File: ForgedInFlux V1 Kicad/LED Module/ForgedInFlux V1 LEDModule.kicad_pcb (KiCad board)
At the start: 2 copper layers, 42 x 82 mm, 31 parts

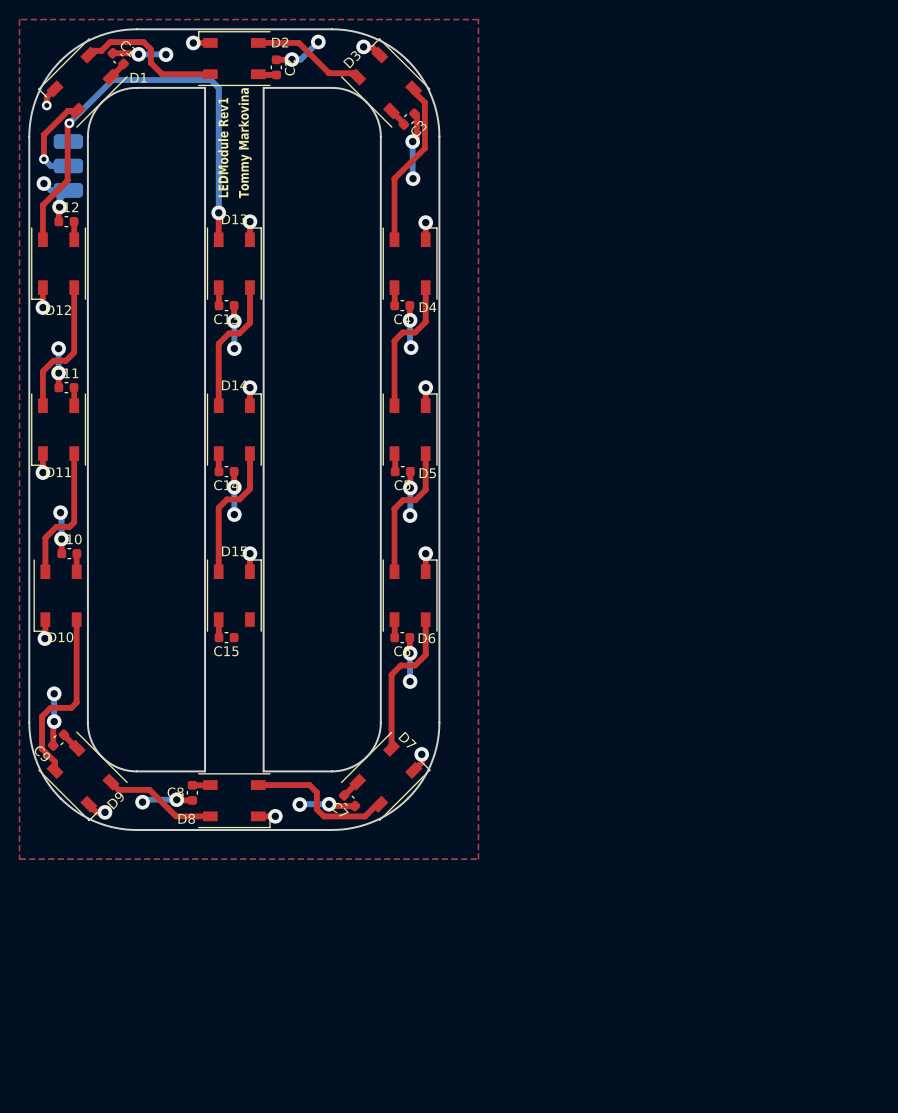
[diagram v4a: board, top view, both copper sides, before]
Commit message: Redesigned PCB
- Components changed for hand solderable parts
- Resistor in future will need to be exchanged for one that can handle more wattage.
- In future more clearance will be needed for top right LED.
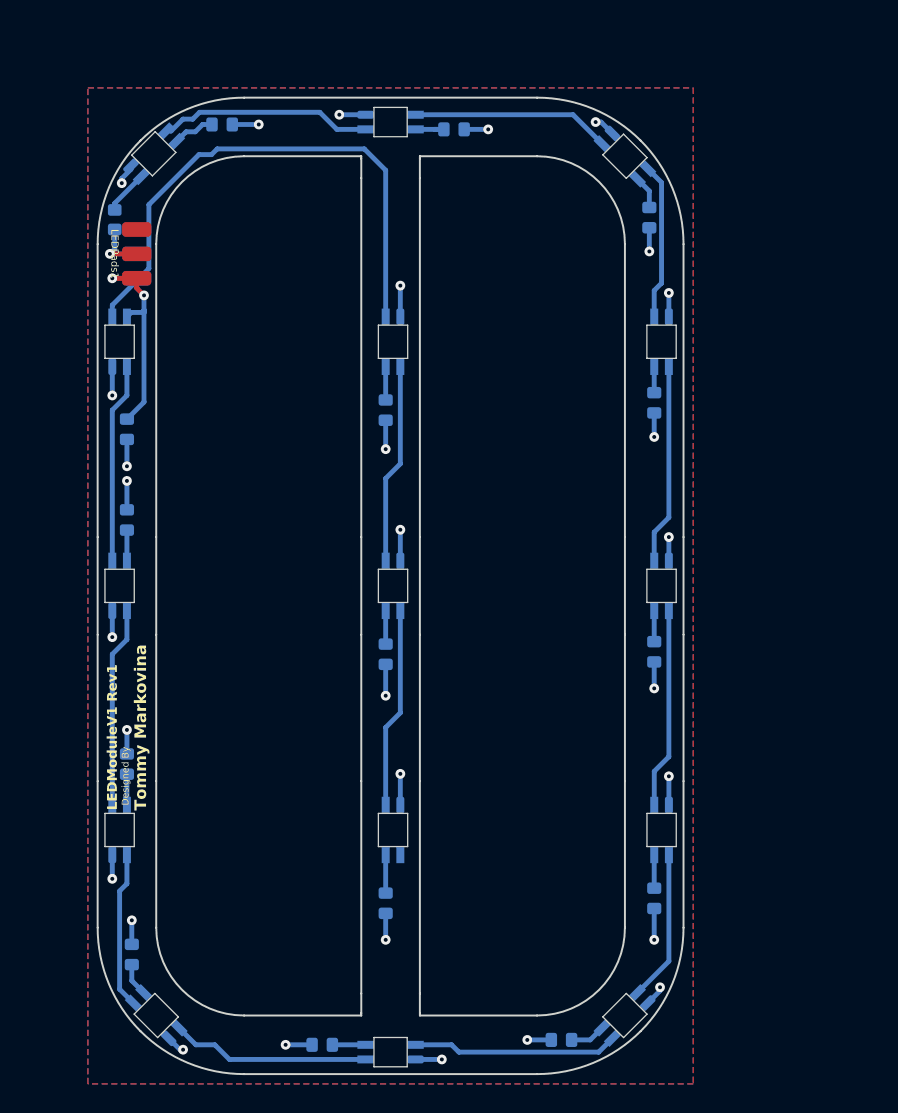
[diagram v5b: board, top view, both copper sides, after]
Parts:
- removed D1, D10, D11, D12, D13, D14, D15, D2, D3, D4, D5, D6, D7, D8, D9: SK6812, LED_SMD:LED_SK6812_PLCC4_5.0x5.0mm_P3.2mm
- added LED1: SK6812MINI-E, LEDModuleLibrary:SK6812-MINI-E, B.Cu at (25.8, 25.8)
- added LED10: SK6812MINI-E, LEDModuleLibrary:SK6812-MINI-E, B.Cu at (22.2, 95.0)
- added LED11: SK6812MINI-E, LEDModuleLibrary:SK6812-MINI-E, B.Cu at (22.2, 70.0)
- added LED12: SK6812MINI-E, LEDModuleLibrary:SK6812-MINI-E, B.Cu at (22.2, 45.0)
- added LED13: SK6812MINI-E, LEDModuleLibrary:SK6812-MINI-E, B.Cu at (50.2, 45.0)
- added LED14: SK6812MINI-E, LEDModuleLibrary:SK6812-MINI-E, B.Cu at (50.2, 70.0)
- added LED15: SK6812MINI-E, LEDModuleLibrary:SK6812-MINI-E, B.Cu at (50.2, 95.0)
- added LED2: SK6812MINI-E, LEDModuleLibrary:SK6812-MINI-E, B.Cu at (50.0, 22.5)
- added LED3: SK6812MINI-E, LEDModuleLibrary:SK6812-MINI-E, B.Cu at (74.0, 26.0)
- added LED4: SK6812MINI-E, LEDModuleLibrary:SK6812-MINI-E, B.Cu at (77.8, 45.0)
- added LED5: SK6812MINI-E, LEDModuleLibrary:SK6812-MINI-E, B.Cu at (77.8, 70.0)
- added LED6: SK6812MINI-E, LEDModuleLibrary:SK6812-MINI-E, B.Cu at (77.8, 95.0)
- added LED7: SK6812MINI-E, LEDModuleLibrary:SK6812-MINI-E, B.Cu at (74.0, 114.0)
- added LED8: SK6812MINI-E, LEDModuleLibrary:SK6812-MINI-E, B.Cu at (50.0, 117.8)
- added LED9: SK6812MINI-E, LEDModuleLibrary:SK6812-MINI-E, B.Cu at (26.0, 114.0)
- added R1: 220R, Resistor_SMD:R_0805_2012Metric_Pad1.20x1.40mm_HandSolder, B.Cu at (21.8, 32.5)
- C1, C10, C11, C12, C13, C14, C15, C2, C3, C4, C5, C6, C7, C8, C9: footprint Capacitor_SMD:C_0603_1608Metric -> Capacitor_SMD:C_0805_2012Metric_Pad1.18x1.45mm_HandSolder; moved to B.Cu
- LEDPads1: moved to F.Cu
- moved C6 37.1 mm to (77.0, 102.0), turned to -90 degrees
- moved C7 32.7 mm to (67.5, 116.5), turned to 180 degrees
- moved C15 31.7 mm to (49.5, 102.5), turned to -90 degrees
- moved C5 31.7 mm to (77.0, 76.8), turned to -90 degrees
- moved C8 29.0 mm to (43.0, 117.0), turned to 180 degrees
- moved C4 27.7 mm to (77.0, 51.2), turned to -90 degrees
- moved C3 26.6 mm to (76.5, 32.3), turned to -90 degrees
- moved C14 24.8 mm to (49.5, 77.0), turned to -90 degrees
- moved C9 23.2 mm to (23.5, 107.8), turned to 90 degrees
- moved C10 22.3 mm to (23.0, 88.2), turned to 90 degrees
- moved C12 22.1 mm to (23.0, 54.0), turned to -90 degrees
- moved C13 19.5 mm to (49.5, 52.0), turned to -90 degrees
- moved C2 19.3 mm to (56.5, 23.2), turned to 0 degrees
- moved C11 14.9 mm to (23.0, 63.2), turned to 90 degrees
- moved C1 12.6 mm to (32.8, 22.8), turned to 0 degrees
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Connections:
- C1 pad 2: Net-(D1-VDD) -> GND
- C10 pad 2: Net-(D10-VDD) -> GND
- C11 pad 2: Net-(D11-VDD) -> GND
- C12 pad 2: Net-(D12-VDD) -> GND
- C13 pad 2: Net-(D13-VDD) -> GND
- C14 pad 2: Net-(D14-VDD) -> GND
- C15 pad 2: Net-(D15-VDD) -> GND
- C2 pad 2: Net-(D2-VDD) -> GND
- C3 pad 2: Net-(D3-VDD) -> GND
- C4 pad 2: Net-(D4-VDD) -> GND
- C5 pad 2: Net-(D5-VDD) -> GND
- C6 pad 2: Net-(D6-VDD) -> GND
- C7 pad 2: Net-(D7-VDD) -> GND
- C8 pad 2: Net-(D8-VDD) -> GND
- C9 pad 2: Net-(D9-VDD) -> GND
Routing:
- net Net-(LED12-DOUT): track 0.00 -> 55.6 mm
- net GND: track 28.5 -> 80.1 mm, vias 15 -> 30
- net Net-(D12-DOUT): track 46.1 -> 0.00 mm, vias 2 -> 0
- net Net-(LED1-DOUT): track 0.00 -> 21.9 mm
- net Net-(LED7-DOUT): track 0.00 -> 21.1 mm
- net Net-(LED13-DOUT): track 0.00 -> 20.5 mm
- net Net-(LED4-DOUT): track 0.00 -> 20.5 mm
- net Net-(LED14-DOUT): track 0.00 -> 20.5 mm
- net Net-(LED11-DOUT): track 0.00 -> 20.5 mm
- net Net-(LED10-DOUT): track 0.00 -> 20.5 mm
- net Net-(LED5-DOUT): track 0.00 -> 20.5 mm
- net Net-(LED8-DOUT): track 0.00 -> 20.5 mm
- net Net-(LED2-DOUT): track 0.00 -> 20.3 mm
- net Net-(D10-DIN): track 18.7 -> 0.00 mm
- net Net-(D3-DOUT): track 17.2 -> 0.00 mm
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- added copper zone on B.Cu, net +5V
- added copper zone on F.Cu, net GND
- removed copper zone on F.Cu, net +5V
- removed copper zone on B.Cu, net GND
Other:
- board size 42 x 82 mm -> 60 x 100 mm
- board text added: "Designed By"
- board text added: "LEDModuleV1 Rev1"
- board text removed: "LEDModule Rev1"

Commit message: Updated design
- Full 1w SMD Resistor
- Satsified tolerances on LEDS and board edgecuts.
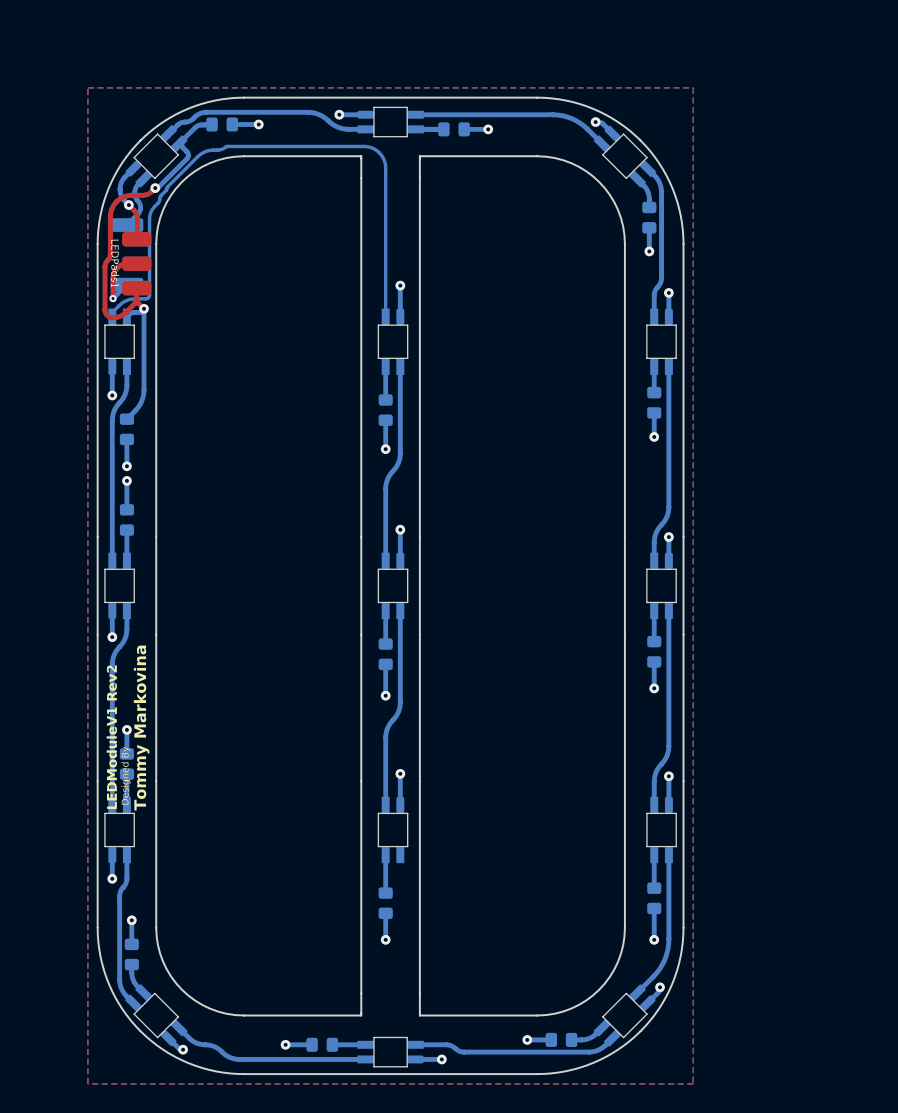
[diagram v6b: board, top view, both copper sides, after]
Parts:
- R1: footprint Resistor_SMD:R_0805_2012Metric_Pad1.20x1.40mm_HandSolder -> Resistor_SMD:R_2512_6332Metric_Pad1.40x3.35mm_HandSolder
- moved R1 3.81 mm to (23.0, 36.1)
- moved LEDPads1 1.00 mm to (24.0, 39.5)
- moved LED1 0.35 mm to (26.0, 26.0)
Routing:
- net +5V: track 67.7 -> 91.7 mm
- net GND: track 80.1 -> 86.2 mm
- net LEDData: track 5.46 -> 7.36 mm
- net Net-(LED1-DIN): track 4.20 -> 5.73 mm
- net Net-(LED12-DOUT): track 55.6 -> 57.0 mm
- net Net-(LED1-DOUT): track 21.9 -> 21.3 mm
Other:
- board text added: "LEDModuleV1 Rev2"
- board text removed: "LEDModuleV1 Rev1"

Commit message: Changes
- removed 1w resistor (not required for sk6812 mini-e leds)
added mounting holes that align with control unit internal standoffs
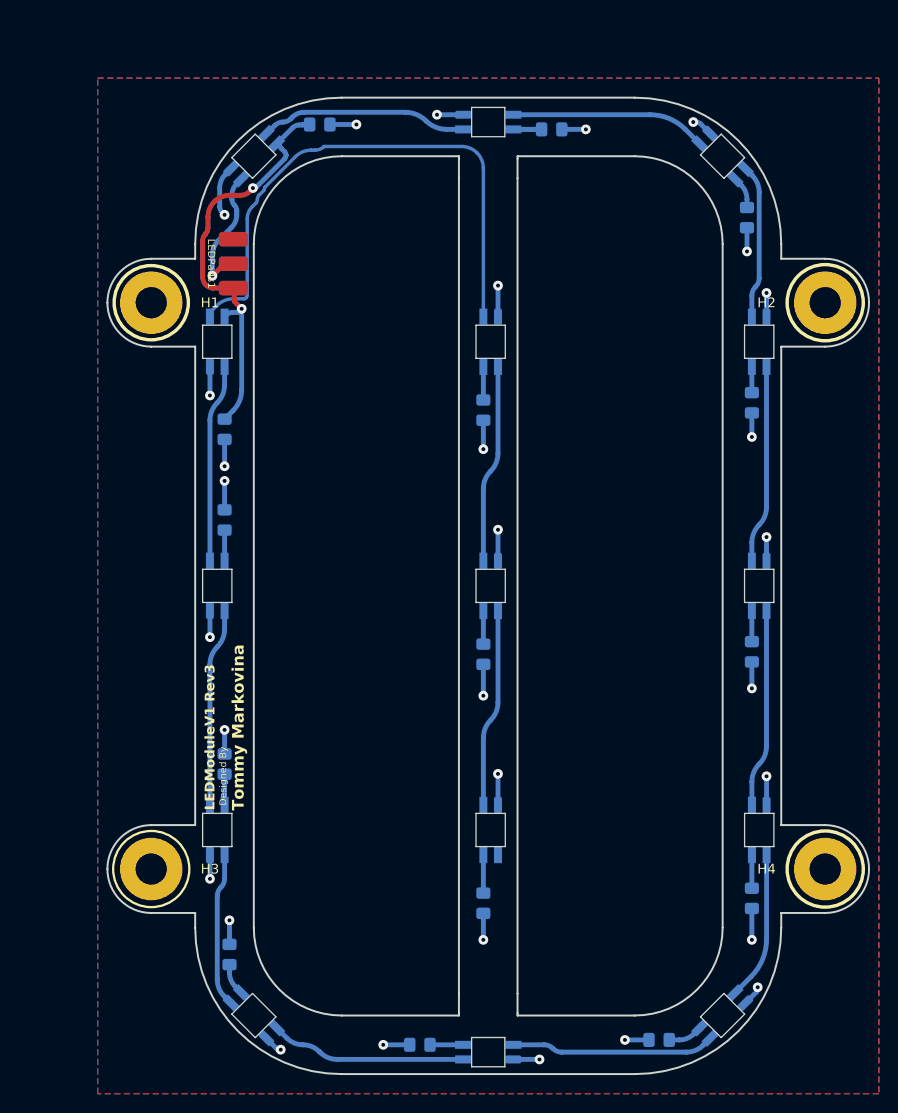
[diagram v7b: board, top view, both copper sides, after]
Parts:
- removed R1: 220R, Resistor_SMD:R_2512_6332Metric_Pad1.40x3.35mm_HandSolder
- added H1: MountingHole, MountingHole:MountingHole_3.2mm_M3_Pad, F.Cu at (25.5, 41.0)
- added H2: MountingHole, MountingHole:MountingHole_3.2mm_M3_Pad, F.Cu at (94.5, 41.0)
- added H3: MountingHole, MountingHole:MountingHole_3.2mm_M3_Pad, F.Cu at (25.5, 99.0)
- added H4: MountingHole, MountingHole:MountingHole_3.2mm_M3_Pad, F.Cu at (94.5, 99.0)
- moved C1 10.0 mm to (42.8, 22.8)
- moved C10 10.0 mm to (33.0, 88.2)
- moved C11 10.0 mm to (33.0, 63.2)
- moved C12 10.0 mm to (33.0, 54.0)
- moved C13 10.0 mm to (59.5, 52.0)
- moved C14 10.0 mm to (59.5, 77.0)
- moved C15 10.0 mm to (59.5, 102.5)
- moved C2 10.0 mm to (66.5, 23.2)
- moved C3 10.0 mm to (86.5, 32.3)
- moved C4 10.0 mm to (87.0, 51.2)
- moved C5 10.0 mm to (87.0, 76.8)
- moved C6 10.0 mm to (87.0, 102.0)
- moved C7 10.0 mm to (77.5, 116.5)
- moved C8 10.0 mm to (53.0, 117.0)
- moved C9 10.0 mm to (33.5, 107.8)
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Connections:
- LED1 pad 4: Net-(LED1-DIN) -> LEDData
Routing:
- net LEDData: track 7.36 -> 14.0 mm
- net Net-(LED1-DIN): track 5.73 -> 0.00 mm
- net +5V: track 91.7 -> 88.0 mm
- net GND: track 86.2 -> 83.2 mm
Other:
- board size 60 x 100 mm -> 78 x 100 mm
- board text added: "LEDModuleV1 Rev3"
- board text removed: "LEDModuleV1 Rev2"
